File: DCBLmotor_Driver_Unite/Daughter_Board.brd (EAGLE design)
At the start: 99.8 x 72.3 mm, 42 parts, among them CN1 FX23L-20P-0.5SV12, CN2 DF63-2P-3.96DSA, CN4 DF63-3P-3.96DSA, IC1 IR25750LPBF, IC2 IR25750LPBF, IC3 IR25750LPBF, IC4 DRV8320SRTVT, IC6 LTM8050IY#PBF-ND

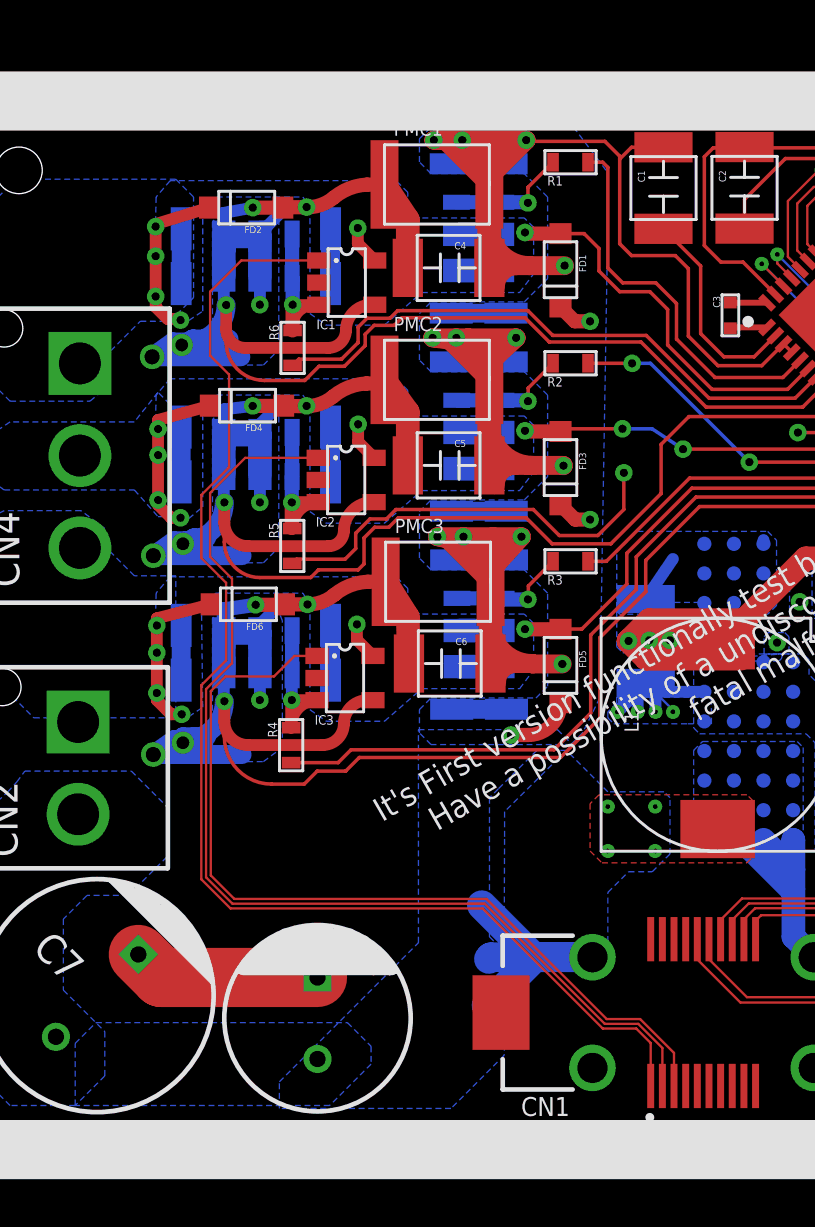
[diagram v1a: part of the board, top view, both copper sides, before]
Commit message: Change to 1 shant
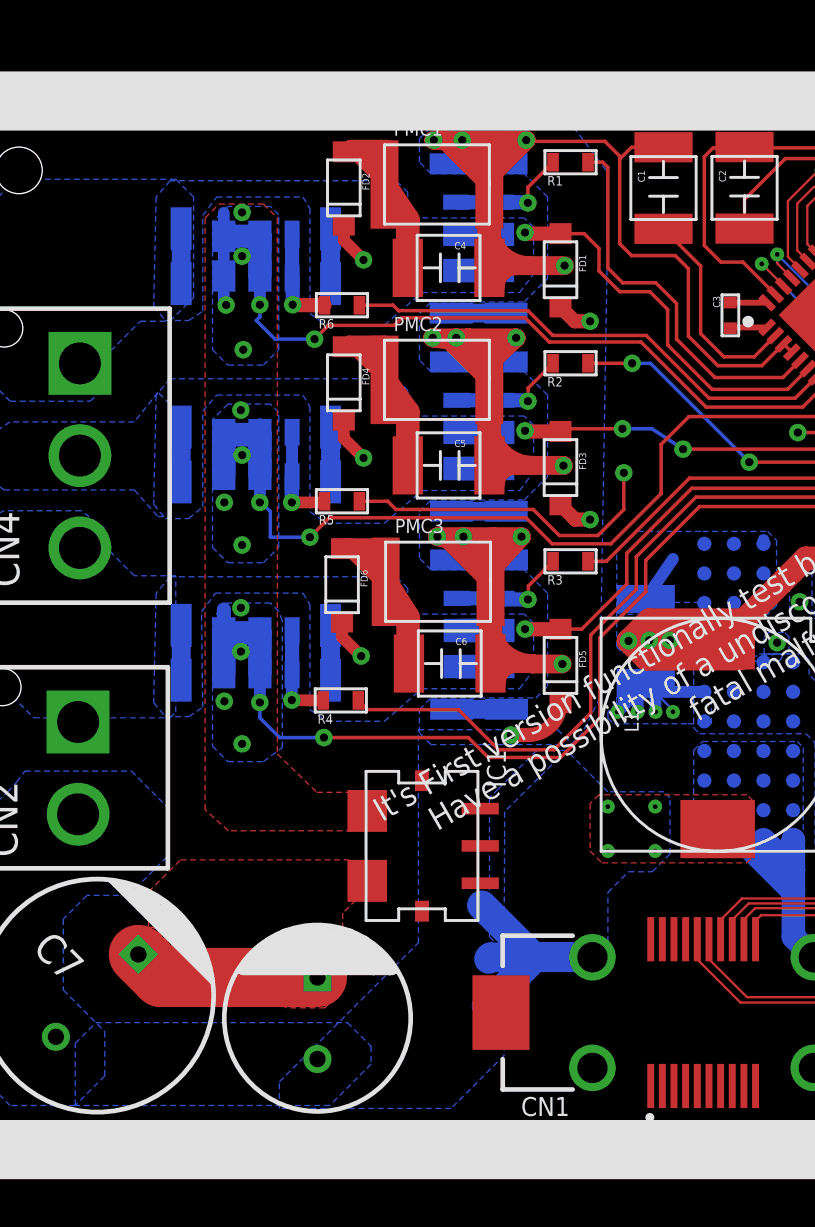
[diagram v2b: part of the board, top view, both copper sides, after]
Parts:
- removed IC2, IC3: IR25750LPBF, Infinion:SOT-23-L5
- IC1: value IR25750LPBF -> ACS780KLRTR-150B-T; device Infinion:SOT-23-L5 -> ACS780:7-PIN_PSOP
- moved IC1 24.4 mm to (45.1, 35.7), turned to 90 degrees
- moved FD2 5.81 mm to (41.8, 62.3), turned to 90 degrees
- moved FD4 5.76 mm to (41.8, 53.9), turned to 90 degrees
- moved FD6 5.67 mm to (41.7, 45.3), turned to 90 degrees
- moved R5 2.87 mm to (41.7, 50.4), turned to 0 degrees
- moved R4 2.87 mm to (41.6, 41.9), turned to 0 degrees
- moved R6 2.80 mm to (41.7, 58.9), turned to 0 degrees
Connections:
- new net LOSIDE: C4.P$2, C5.P$2, C6.P$2, FD2.A, FD4.A, FD6.A, FET2.S1, FET2.S2, FET2.S3, FET2.S4, FET4.S1, FET4.S2, FET4.S3, FET4.S4, FET6.S1, FET6.S2, FET6.S3, FET6.S4, IC1.P$5, IC4.16, IC4.8, IC4.9, PMC1.P$2, PMC2.P$2, PMC3.P$2
- net CU1: now also IC1.P$3; no longer IC1.P$1
- net CU2: no longer IC2.P$1
- net CU3: no longer IC3.P$1
- net GND: now also IC1.P$6; no longer C4.P$2, C5.P$2, C6.P$2, FD2.A, FD4.A, FD6.A, FET2.S1, FET2.S2, FET2.S3, FET2.S4, FET4.S1, FET4.S2, FET4.S3, FET4.S4, FET6.S1, FET6.S2, FET6.S3, FET6.S4, IC1.P$4, IC2.P$4, IC3.P$4, IC4.16, IC4.8, IC4.9, PMC1.P$2, PMC2.P$2, PMC3.P$2
- net N$18: no longer IC3.P$3
- net N$2: no longer IC2.P$3
- net N$4: no longer IC1.P$3
- net VS1: no longer IC1.P$5
- net VS2: no longer IC2.P$5
- net VS3: no longer IC3.P$5
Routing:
- net GND: track 265.6 -> 29.5 mm, vias 29 -> 11
- net LOSIDE: track 0.00 -> 160.0 mm, vias 0 -> 18
- net CU1: track 56.2 -> 0.00 mm
- net CU2: track 46.9 -> 0.00 mm
- net CU3: track 37.5 -> 0.00 mm
- net VS1: track 33.9 -> 26.7 mm, vias 6 -> 2
- net VS3: track 42.3 -> 35.3 mm, vias 6 -> 2
- net VS2: track 36.0 -> 29.0 mm, vias 8 -> 4
- net LO1: track 25.8 -> 21.6 mm
- net LO2: track 32.0 -> 27.9 mm
- net N$18: track 6.93 -> 4.41 mm
- net N$4: track 6.73 -> 4.43 mm
- net LO3: track 40.7 -> 38.5 mm
- net N$2: track 6.90 -> 4.87 mm
- added copper zone on layer 1, net GND
- added copper zone on layer 1, net LOSIDE
- added copper zone on layer 16, net LOSIDE

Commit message: Main_borad is Almost_finshed
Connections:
- removed net AGND: C2.P$1, IC4.23, IC4.31
- net GND: now also C2.P$1, IC4.23, IC4.31
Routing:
- net AGND: track 19.8 -> 0.00 mm
- net CU1: track 0.00 -> 17.5 mm
- net GND: track 29.5 -> 43.0 mm, vias 11 -> 13
- net +3.3V: track 10.8 -> 19.0 mm, vias 0 -> 2
- removed copper zone on layer 3, net +3.3V
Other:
- board size 99.8 x 72.3 mm -> 53.5 x 50.6 mm
- board text added: "+3.3V"
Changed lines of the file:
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@@
 <board>
 <plain>
-<wire x1="0.2" y1="7.7" x2="99.85" y2="7.7" width="0" layer="20"/>
-<wire x1="99.85" y1="7.7" x2="99.85" y2="79.9" width="0" layer="20"/>
-<wire x1="99.85" y1="79.9" x2="0.1" y2="80" width="0" layer="20"/>
-<wire x1="0.1" y1="80" x2="0.2" y2="7.7" width="0" layer="20"/>
-<text x="52.525" y="12.2" size="1.27" layer="22" rot="MR0">It's First version functionally test board
-Have a possibility of a undiscovered fatal malfunction</text>
-<text x="52.575" y="9" size="2.54" layer="22" rot="MR0">CAUTION</text>
-<hole x="3.5" y="11" drill="3.4"/>
-<hole x="3.5" y="75" drill="3.4"/>
-<hole x="97" y="75" drill="3.4"/>
-<hole x="97" y="10.5" drill="3.4"/>
+<wire x1="18.1324" y1="19.2824" x2="71.6052" y2="19.1808" width="0" layer="20"/>
+<wire x1="71.6052" y1="19.1808" x2="71.5036" y2="69.6892" width="0" layer="20"/>
+<wire x1="71.5036" y1="69.6892" x2="18.2356" y2="69.7892" width="0" layer="20"/>
+<wire x1="18.2356" y1="69.7892" x2="18.1324" y2="19.2824" width="0" layer="20"/>
 <wire x1="24.651" y1="67.619" x2="69.651" y2="67.619" width="2.54" layer="21"/>
 <wire x1="69.651" y1="67.619" x2="69.651" y2="22.619" width="2.54" layer="21"/>
@@
 <dimension x1="45" y1="28" x2="68" y2="28" x3="56.5" y3="12" textsize="1.778" layer="1"/>
 <dimension x1="48" y1="24" x2="48" y2="35" x3="17" y3="29.5" textsize="1.778" layer="1"/>
+<text x="66.9544" y="64.5668" size="0.4064" layer="21" rot="R90">+3.3V</text>
 </plain>
 <attributes>
@@
 </polygon>
 <contactref element="IC4" pad="33"/>
-<wire x1="62.9244" y1="55.958721875" x2="62.9244" y2="56.3372" width="0.2032" layer="1"/>
-<wire x1="62.9244" y1="56.3372" x2="62.9244" y2="56.388" width="0.2032" layer="1"/>
-<wire x1="63.0483625" y1="56.2132375" x2="62.9244" y2="56.3372" width="0.2032" layer="1"/>
-<wire x1="62.791840625" y1="56.255440625" x2="62.9244" y2="56.388" width="0.2032" layer="1"/>
 <contactref element="C7" pad="P$-"/>
 <contactref element="CN2" pad="P$1"/>
 <wire x1="32.93536875" y1="30.994446875" x2="33.923753125" y2="30.0060625" width="2.54" layer="1"/>
 <wire x1="33.923753125" y1="30.0060625" x2="40.624609375" y2="30.0060625" width="2.54" layer="1"/>
-<wire x1="62.9244" y1="54.959575" x2="62.9231125" y2="54.9582875" width="0.508" layer="1"/>
-<via x="62.9231125" y="54.9582875" extent="1-16" drill="0.35"/>
-<wire x1="62.9231125" y1="54.9582875" x2="63.04685625" y2="54.83454375" width="0.508" layer="2"/>
-<wire x1="63.04685625" y1="54.83454375" x2="62.7461125" y2="54.5338" width="0.508" layer="2"/>
-<wire x1="62.7461125" y1="54.5338" x2="62.4078" y2="54.5338" width="0.508" layer="2"/>
-<wire x1="62.9244" y1="58.4336" x2="62.9244" y2="54.959575" width="0.1524" layer="1"/>
 <contactref element="IC6" pad="C5"/>
 <contactref element="IC6" pad="C7"/>
@@
 <vertex x="42.2656" y="34.7472"/>
 </polygon>
-<wire x1="62.9231125" y1="54.9582875" x2="62.9244" y2="55.958721875" width="0" layer="19" extent="1-2"/>
+<via x="67.2084" y="63.5" extent="1-16" drill="0.75"/>
+<contactref element="C2" pad="P$1"/>
+<contactref element="IC4" pad="23"/>
+<contactref element="IC4" pad="31"/>
+<wire x1="63.5254" y1="65.6082" x2="59.436" y2="65.6082" width="0.1524" layer="1"/>
+<wire x1="60.272746875" y1="59.31748125" x2="59.5919125" y2="59.998315625" width="0.1524" layer="1"/>
+<wire x1="64.77" y1="62.04696875" x2="64.77" y2="64.3636" width="0.1524" layer="1"/>
+<wire x1="64.77" y1="64.3636" x2="63.5254" y2="65.6082" width="0.1524" layer="1"/>
+<wire x1="63.80828125" y1="61.08525" x2="64.77" y2="62.04696875" width="0.1524" layer="1"/>
+<wire x1="60.272746875" y1="59.31748125" x2="61.156628125" y2="58.4336" width="0.254" layer="1"/>
+<wire x1="61.156628125" y1="58.4336" x2="62.9244" y2="58.4336" width="0.254" layer="1"/>
+<wire x1="58.985709375" y1="65.6082" x2="59.436" y2="65.6082" width="0.254" layer="1"/>
+<wire x1="59.5919125" y1="59.998315625" x2="58.213284375" y2="59.998315625" width="0.1524" layer="1"/>
+<wire x1="58.213284375" y1="59.998315625" x2="58.1152" y2="60.0964" width="0.1524" layer="1"/>
+<via x="58.1152" y="60.0964" extent="1-16" drill="0.25"/>
+<wire x1="58.1152" y1="60.0964" x2="57.9374" y2="60.2742" width="0.1524" layer="1"/>
+<wire x1="58.95159375" y1="65.642315625" x2="57.2008" y2="63.891521875" width="0.1524" layer="1"/>
+<wire x1="57.2008" y1="63.891521875" x2="57.2008" y2="63.4492" width="0.1524" layer="1"/>
+<via x="57.2008" y="63.4492" extent="1-16" drill="0.25"/>
+<wire x1="58.95159375" y1="65.642315625" x2="58.985709375" y2="65.6082" width="0" layer="19" extent="1-1"/>
 </signal>
 <signal name="+3.3V">
@@
 <wire x1="64.389" y1="64.008" x2="63.246" y2="65.151" width="0.1524" layer="1"/>
 <wire x1="63.246" y1="65.151" x2="60.706" y2="65.151" width="0.1524" layer="1"/>
-<polygon width="0.254" layer="3" isolate="0.4064">
-<vertex x="23.3934" y="70.7898"/>
-<vertex x="71.0946" y="70.7898"/>
-<vertex x="74.803" y="67.0814"/>
-<vertex x="74.803" y="20.447"/>
-<vertex x="70.6882" y="16.3322"/>
-<vertex x="25.9842" y="16.3322"/>
-<vertex x="20.2184" y="22.098"/>
-<vertex x="20.2184" y="67.6148"/>
-</polygon>
+<via x="65.7352" y="65.3796" extent="1-16" drill="0.75"/>
+<wire x1="58.95159375" y1="63.39659375" x2="58.95159375" y2="64.246115625" width="0.1524" layer="1"/>
+<wire x1="58.95159375" y1="64.246115625" x2="58.928" y2="64.269709375" width="0.1524" layer="1"/>
+<via x="58.928" y="64.269709375" extent="1-16" drill="0.4" shape="square"/>
+<wire x1="58.928" y1="64.269709375" x2="58.928" y2="64.262" width="0.1524" layer="3"/>
+<wire x1="58.928" y1="64.269709375" x2="60.037890625" y2="65.3796" width="0.508" layer="3"/>
+<wire x1="60.037890625" y1="65.3796" x2="65.7352" y2="65.3796" width="0.508" layer="3"/>
 </signal>
 <signal name="CU3">
@@
 <contactref element="CN1" pad="1"/>
 <contactref element="IC1" pad="P$3"/>
-<wire x1="54.9254" y1="25.3488" x2="47.6096" y2="37.2508" width="0" layer="19" extent="1-1"/>
+<wire x1="47.6096" y1="37.2508" x2="49.668" y2="37.2508" width="0.1524" layer="1"/>
+<wire x1="49.668" y1="37.2508" x2="50.6476" y2="36.2712" width="0.1524" layer="1"/>
+<wire x1="50.6476" y1="36.2712" x2="50.6476" y2="29.4132" width="0.1524" layer="1"/>
+<wire x1="50.6476" y1="29.4132" x2="51.816" y2="28.2448" width="0.1524" layer="1"/>
+<wire x1="51.816" y1="28.2448" x2="54.0512" y2="28.2448" width="0.1524" layer="1"/>
+<wire x1="54.0512" y1="28.2448" x2="54.9656" y2="27.3304" width="0.1524" layer="1"/>
+<wire x1="54.9656" y1="27.3304" x2="54.9254" y2="27.2902" width="0.1524" layer="1"/>
+<wire x1="54.9254" y1="27.2902" x2="54.9254" y2="25.3488" width="0.1524" layer="1"/>
 </signal>
 <signal name="VCC">
@@
 <wire x1="57.0686" y1="57.6378" x2="57.0686" y2="60.5386" width="0.1524" layer="1"/>
 </signal>
-<signal name="AGND">
-<contactref element="C2" pad="P$1"/>
-<contactref element="IC4" pad="23"/>
-<contactref element="IC4" pad="31"/>
-<wire x1="58.95159375" y1="65.642315625" x2="59.138109375" y2="65.6082" width="0.1524" layer="1"/>
-<wire x1="59.138109375" y1="65.6082" x2="57.6072" y2="65.6082" width="0.1524" layer="1"/>
-<wire x1="63.5254" y1="65.6082" x2="59.138109375" y2="65.6082" width="0.1524" layer="1"/>
-<wire x1="60.272746875" y1="59.31748125" x2="58.884228125" y2="60.706" width="0.1524" layer="1"/>
-<wire x1="57.2262" y1="65.2272" x2="57.6072" y2="65.6082" width="0.1524" layer="1"/>
-<wire x1="57.2262" y1="61.4172" x2="57.2262" y2="65.2272" width="0.1524" layer="1"/>
-<wire x1="58.884228125" y1="60.706" x2="57.9374" y2="60.706" width="0.1524" layer="1"/>
-<wire x1="57.9374" y1="60.706" x2="57.2262" y2="61.4172" width="0.1524" layer="1"/>
-<wire x1="63.80828125" y1="61.08525" x2="64.77" y2="62.04696875" width="0.1524" layer="1"/>
-<wire x1="64.77" y1="62.04696875" x2="64.77" y2="64.3636" width="0.1524" layer="1"/>
-<wire x1="64.77" y1="64.3636" x2="63.5254" y2="65.6082" width="0.1524" layer="1"/>
-</signal>
 <signal name="N$7">
